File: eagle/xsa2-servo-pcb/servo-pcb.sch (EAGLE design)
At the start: 36 parts, among them IC1 ESP32-WROOM-32D__4MB_PS_, IC2 FT231XS-R, IC3 NJM2884U1-33-TE1, IC4 TPA2006D1DRBR, IC5 ISL90728UIE627Z-TK, J1 WJEK254-2.54-02P-140-00A, J2 CX70M-24P1, J3 WJEK254-2.54-02P-140-00A, J4 WJEK254-2.54-02P-140-00A, Q1 IRLML6402TRPBF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

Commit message: [eagle] 基板設計追加
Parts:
- added JP1: SERVO1, pinhead:PINHD-1X3/90
- added JP2: SERVO2, pinhead:PINHD-1X3/90
- added JP3: SERVO3, pinhead:PINHD-1X3/90
- added JP4: SERVO4, pinhead:PINHD-1X3/90
- added JP5: (no value), pinhead:PINHD-2X6
- added R15, R16: 1k, rcl:R-US_R0603
- added S2: IS-2235, SamacSys_Parts:IS-2235
- C1, C2, C3, C4, C5, C6, C7, C8, C9: device rcl:C-USC0603 -> rcl:C-EUC0603
- Q1: value IRLML6402TRPBF -> IRLML6402; device SamacSys_Parts:IRLML6402TRPBF -> SamacSys_Parts:IRLML6402
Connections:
- new net N$30: IC1.IO26, JP1.1
- new net N$31: IC1.IO27, JP2.1
- new net N$32: IC1.IO32, JP3.1
- new net N$33: IC1.IO33, JP4.1
- new net N$34: IC1.IO16, JP5.8
- new net N$35: IC2.DTR#, JP5.6
- new net N$36: IC1.IO17, JP5.9
- new net N$37: IC1.IO4, JP5.10
- new net N$38: IC1.IO5, JP5.11
- net +3V3: now also JP5.7, R15.2, R16.2
- net GND: now also JP1.3, JP2.3, JP3.3, JP4.3, JP5.1
- net N$16: now also JP5.5
- net N$17: now also JP5.4
- net N$23: now also JP5.3, R15.1
- net N$24: now also JP5.2, R16.1
- net VDD: now also JP1.2, JP2.2, JP3.2, JP4.2, JP5.12
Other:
- moved on the sheet: C1, C2, IC3, J3, J4, R1, R2, S1

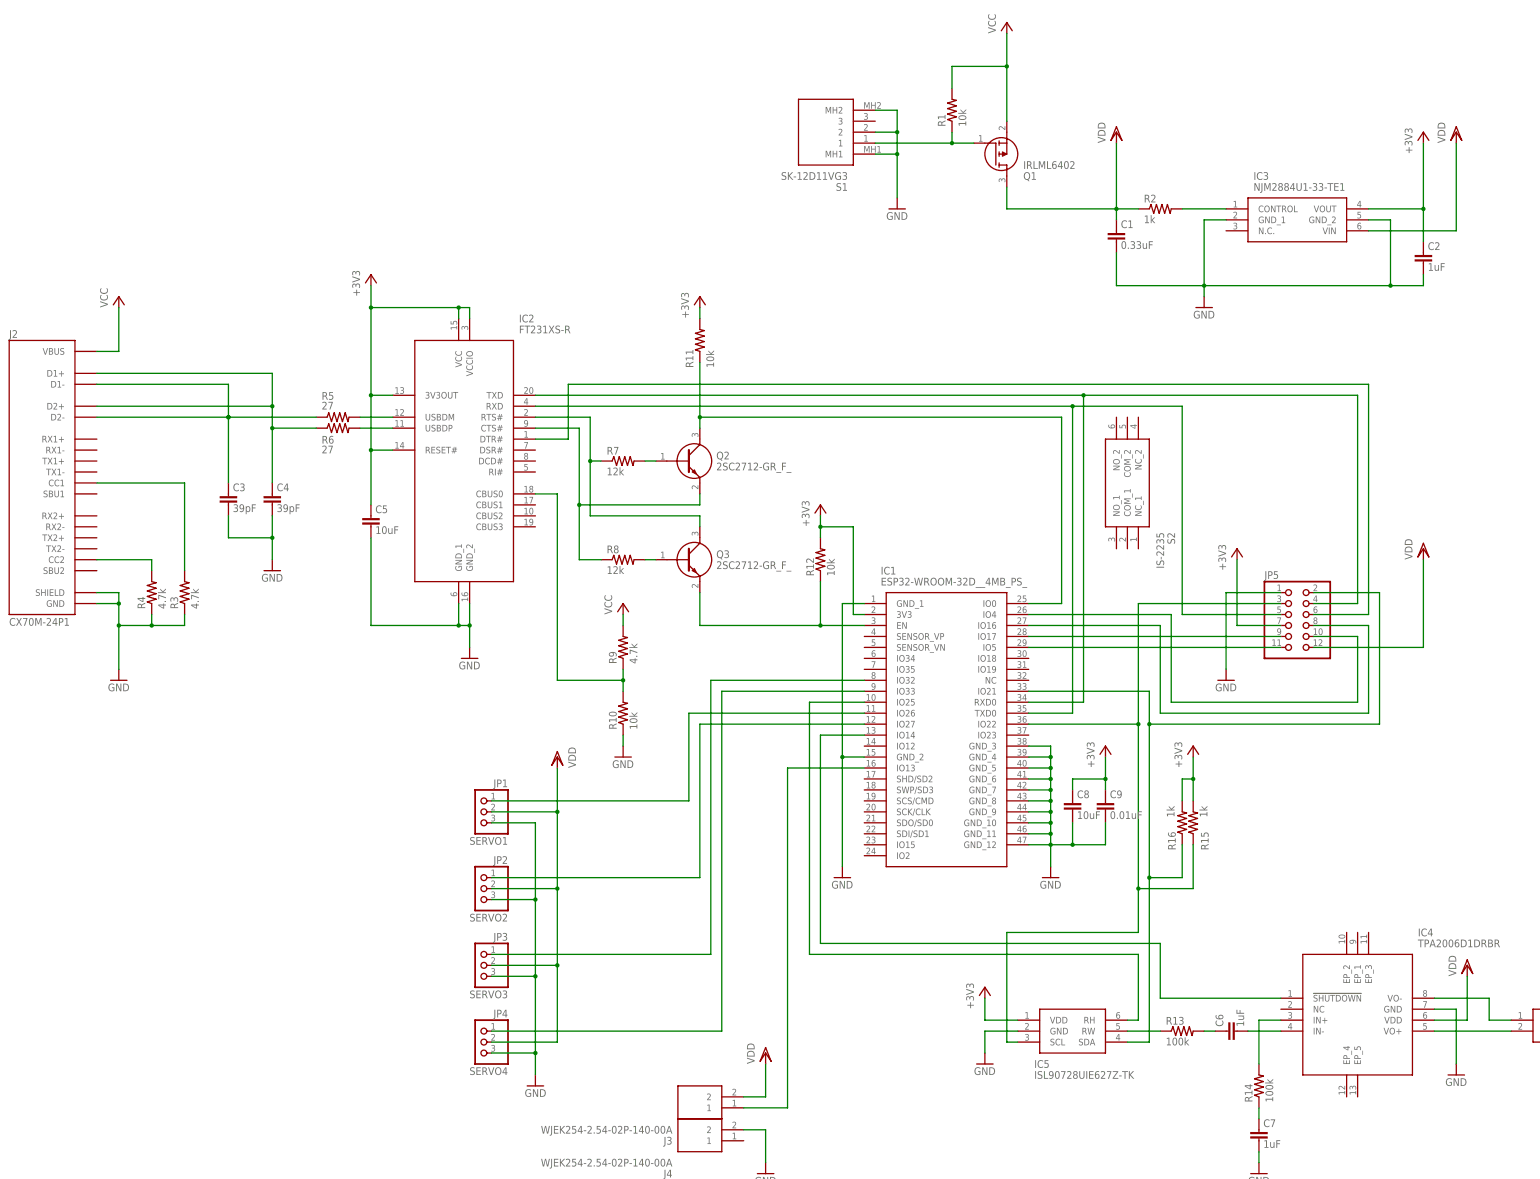
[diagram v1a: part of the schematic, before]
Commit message: [eagle] 回路追加
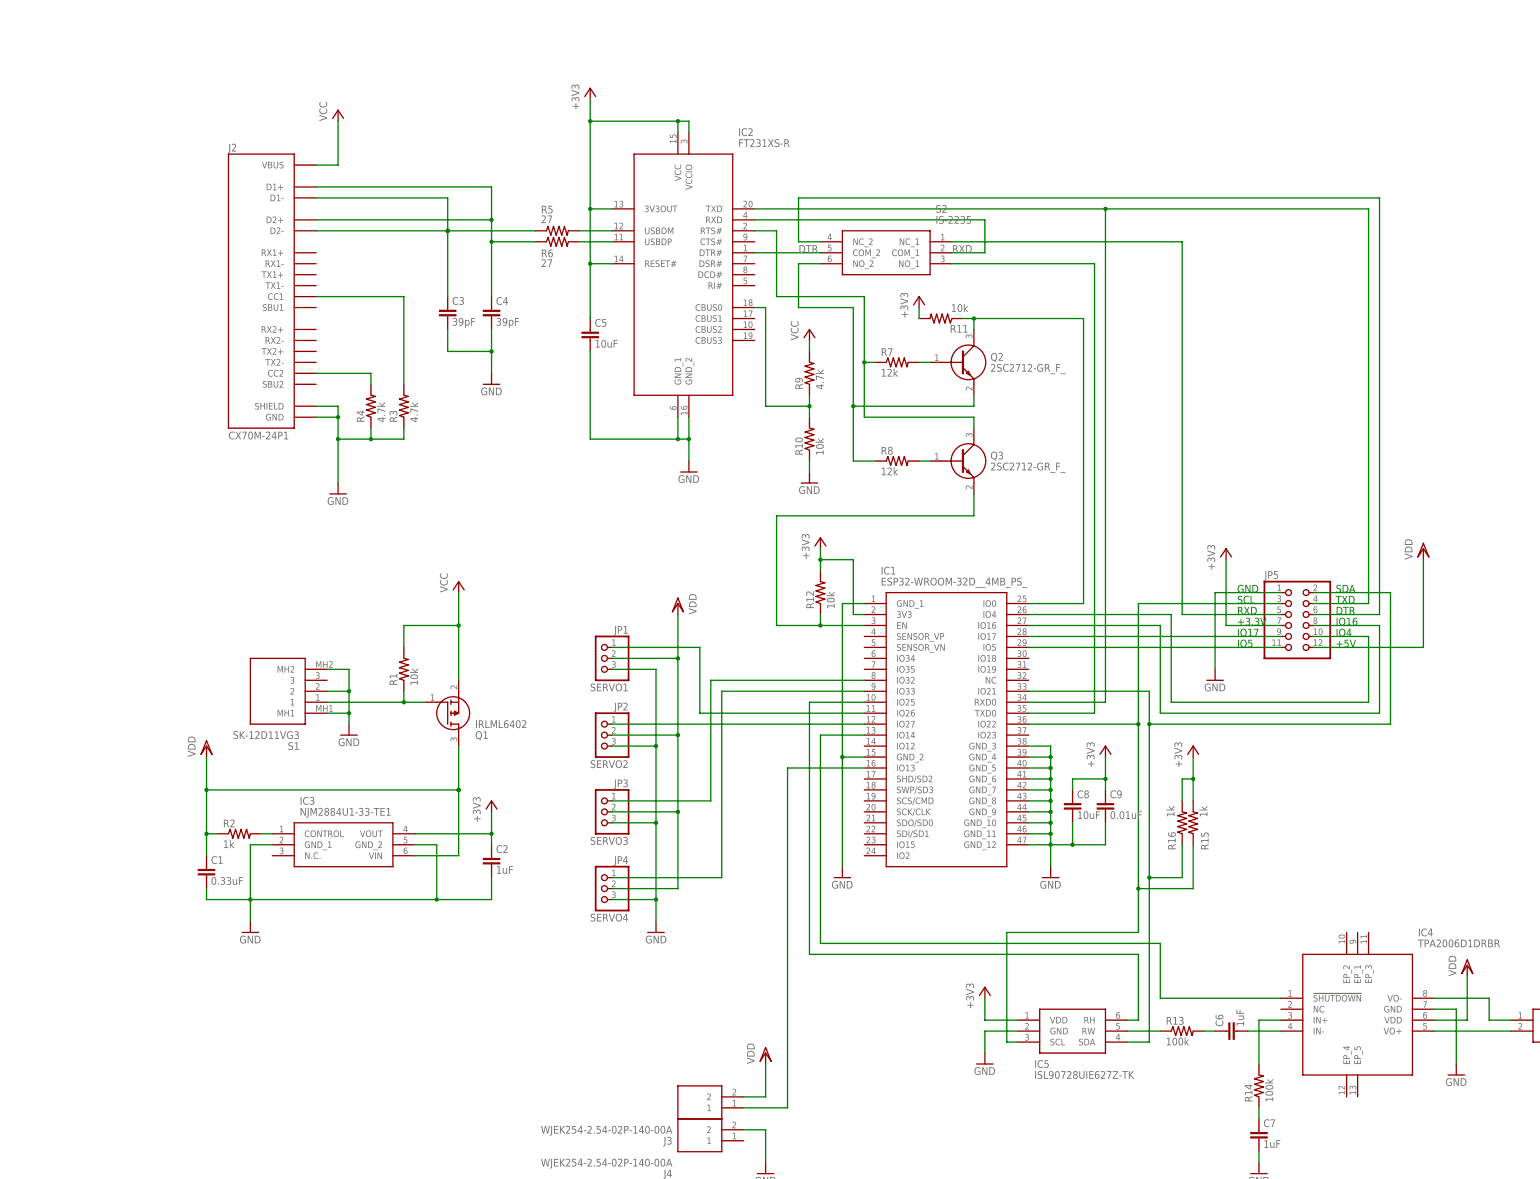
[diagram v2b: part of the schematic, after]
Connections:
- removed net N$35: IC2.DTR#, JP5.6
- new net DTR: IC2.DTR#, S2.COM_2
- new net N$17: JP5.6, S2.NC_2
- new net N$41: JP5.5, S2.NC_1
- new net RXD: IC2.RXD, S2.COM_1
- net N$11: now also S2.NO_2; no longer IC2.CTS#
- net N$16: now also S2.NO_1; no longer IC2.RXD, JP5.5
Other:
- note added: "+3.3V"
- note added: "+5V"
- note added: "DTR"
- note added: "GND"
- note added: "IO16"
- note added: "IO17"
- note added: "IO4"
- note added: "IO5"
- note added: "RXD"
- note added: "SCL"
- note added: "SDA"
- note added: "TXD"
- moved on the sheet: C1, C2, C3, C4, C5, IC2, IC3, J2, JP1, JP2, JP3, JP4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

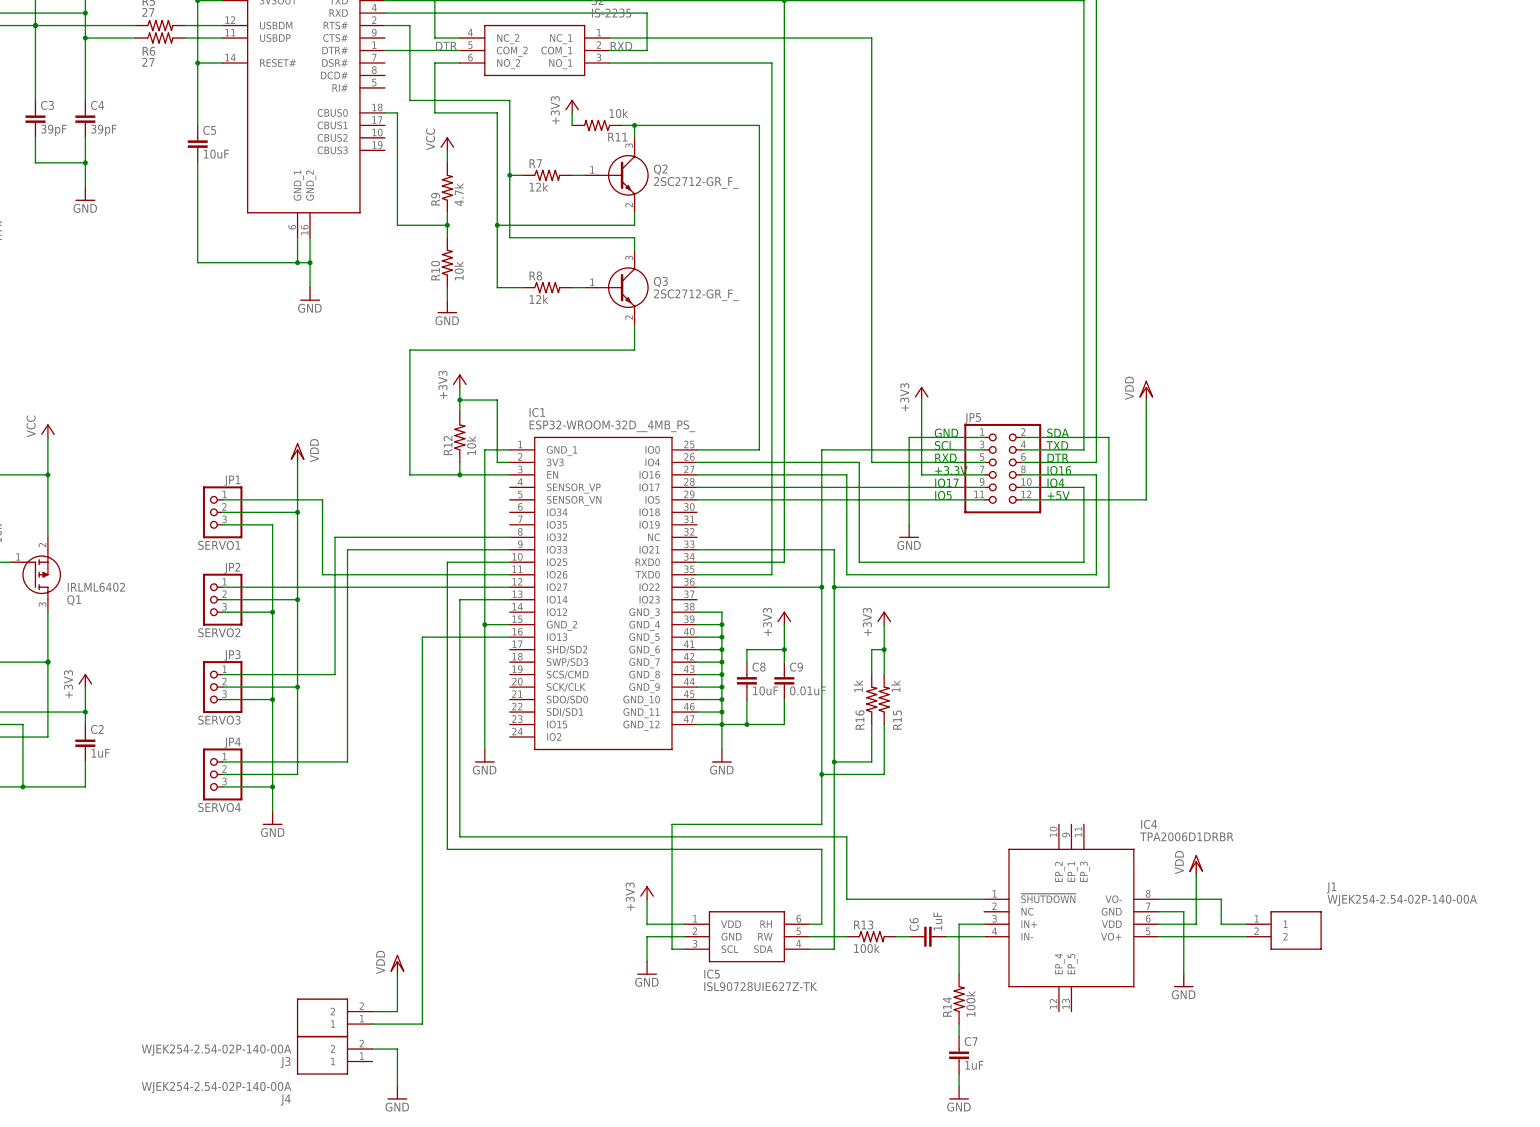
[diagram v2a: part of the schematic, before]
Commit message: [eagle] AVRの赤外受光ピンを変更
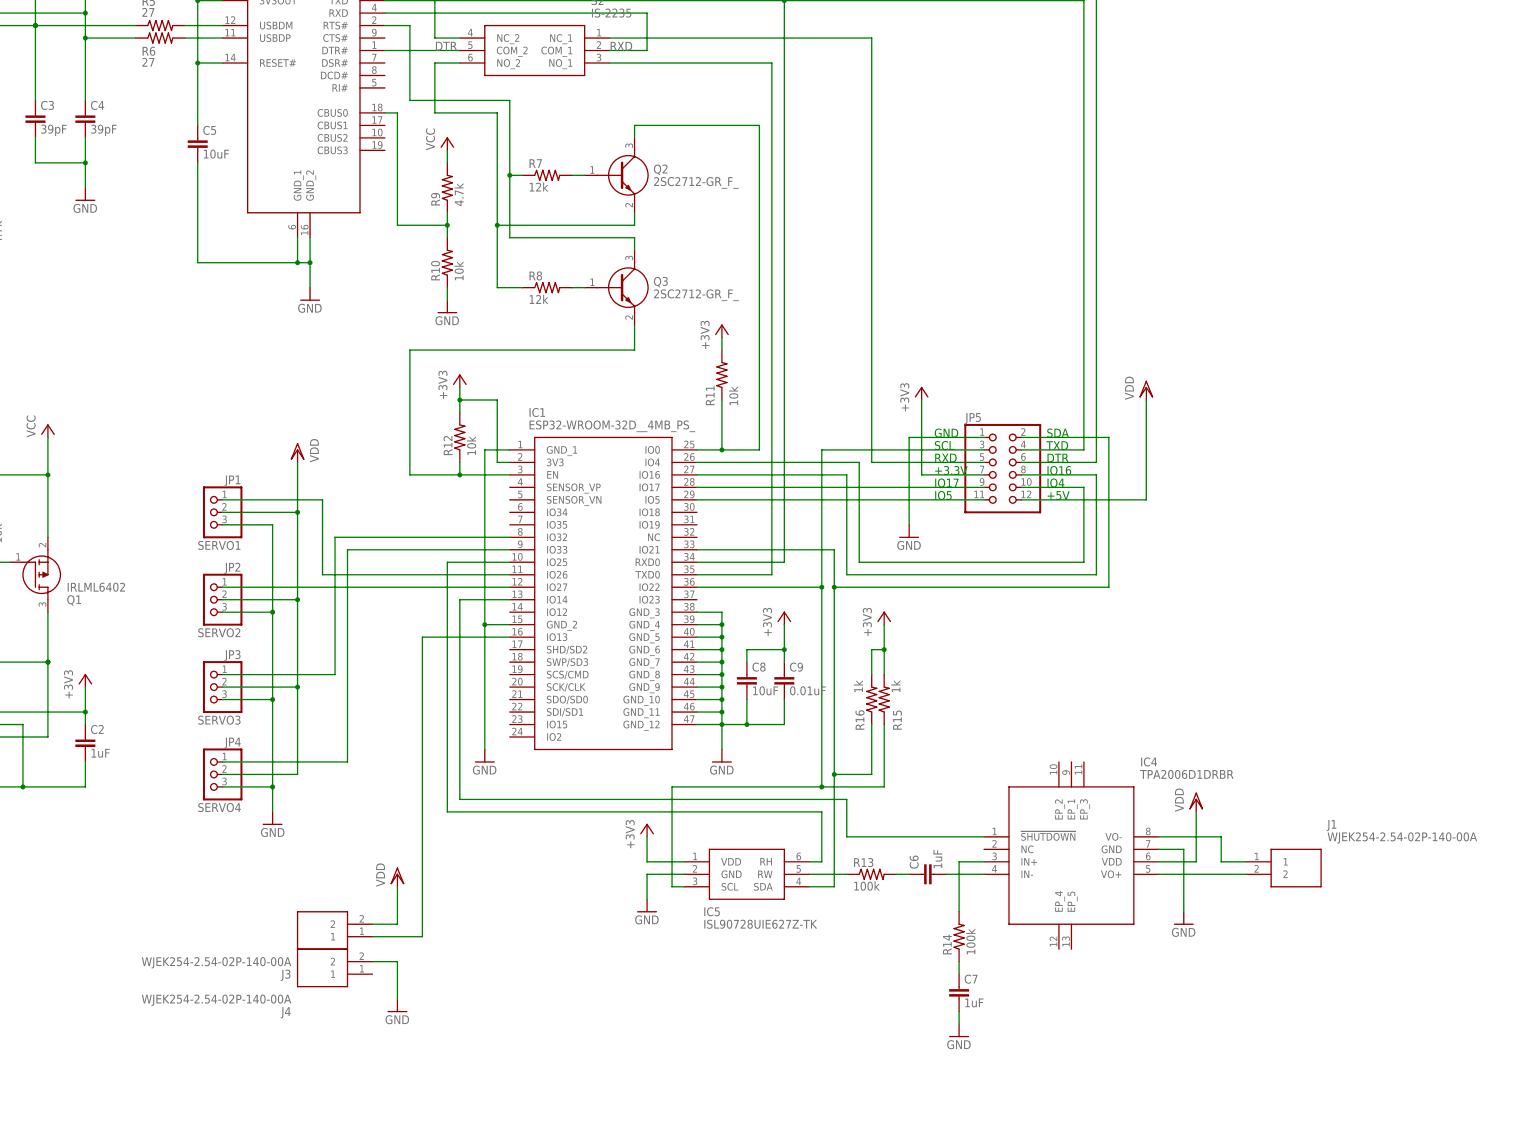
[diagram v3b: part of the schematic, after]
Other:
- moved on the sheet: C6, C7, IC4, IC5, J1, J3, J4, R11, R13, R14

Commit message: [eagle] 回路図更新
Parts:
- removed J2: CX70M-24P1, CX70M-24P1:CX70M-24P1
- added U$1: 5077CR-16-SMC2-BK-TR, FaBo-Connetor:5077CR-16-SMC2-BK-TR
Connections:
- removed net N$4: J2.CC2, R4.2
- removed net N$6: J2.CC1, R3.2
- new net N$35: R4.2, U$1.B5_CC2
- new net N$42: R3.2, U$1.A5_CC1
- net GND: now also U$1.A1,B12_GND, U$1.B1,A12_GND; no longer J2.GND, J2.SHIELD
- net N$1: now also U$1.A6_DP1, U$1.B6_DP2; no longer J2.D1+, J2.D2+
- net N$5: now also U$1.A7_DN1, U$1.B7_DN2; no longer J2.D1-, J2.D2-
- net VCC: now also U$1.A4,B9_VBUS; no longer J2.VBUS
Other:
- note added: "5077CR-16SMC2-BK-TR"
- moved on the sheet: C1, C2, C3, C4, C5, C6, C7, C8, C9, IC1, IC2, IC3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
